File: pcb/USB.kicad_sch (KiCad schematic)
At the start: 101 parts, among them J0 12401598E4#2A, J2 1003-002-01100, J3 1003-002-01100, J4 12401598E4#2A, J5 12401598E4#2A, U0 USBLC6-2SC6, U10 AP22811AW5-7, U11 PTN5110NHQZ, U12 PTN5110NHQZ, U13 PTN5110NHQZ, U14 SN74LVC1G08DCKR, U15 CBTL02043ABQ,115, U19 SN74LVC1G08DCKR, U2 USB7206T/KDX, U20 AP22811AW5-7, U21 USBLC6-2SC6, U23 AP22811AW5-7, U3 CBTL02043ABQ,115, U5 USBLC6-2SC6, U6 CBTL02043ABQ,115, U7 USBLC6-2SC6, U8 USBLC6-2SC6, U9 AP22811AW5-7, X1 ECS-3225MV-250-BN-TR

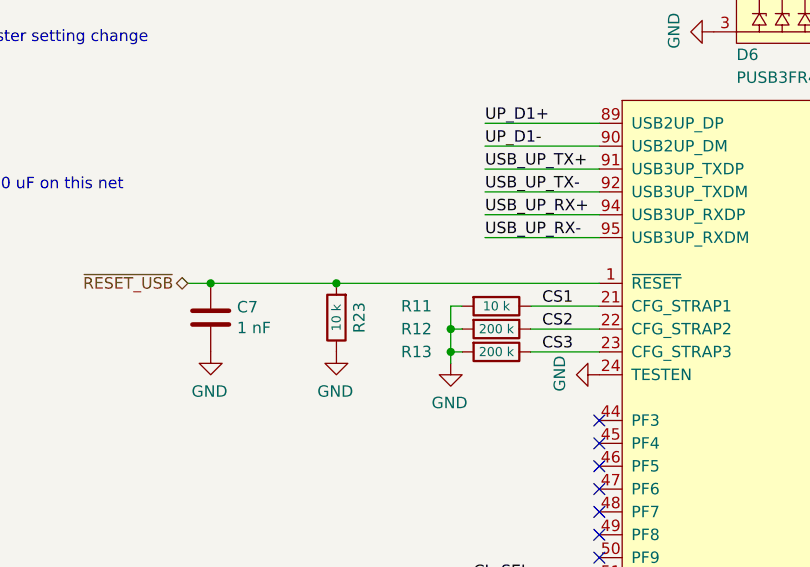
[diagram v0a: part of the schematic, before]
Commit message: hub reset handled by DC-DC power good switch to TLV62585P DC-DC for power good remove reset button - can just plug cable add buttons to ground SDA, SCL as hub bypass to allow programming
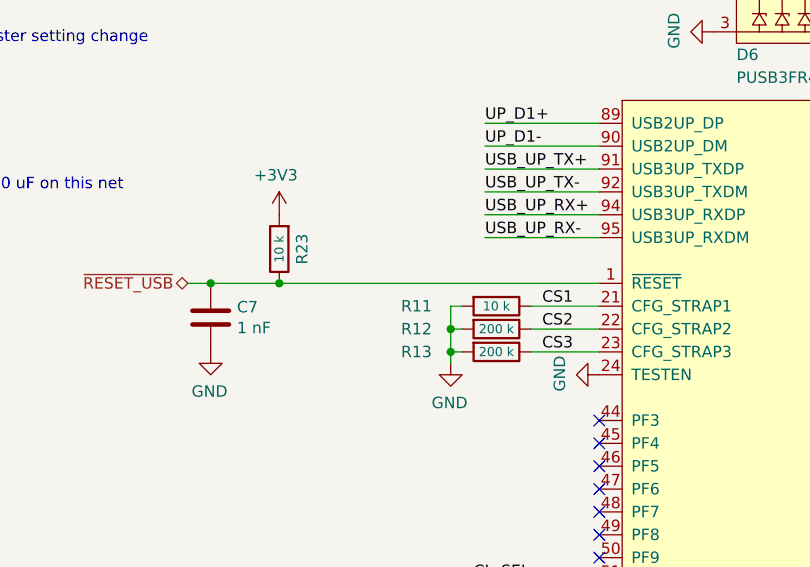
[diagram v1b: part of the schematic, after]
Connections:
- net +3V3: now also R23.2
- net GND: no longer R23.1
- net ~{RESET_USB}: now also R23.1; no longer R23.2
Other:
- moved on the sheet: R23
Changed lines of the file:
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@@
   (junction (at 208.28 226.06) (diameter 0) (color 0 0 0 0)
   )
-  (junction (at 158.75 86.36) (diameter 0) (color 0 0 0 0)
-  )
   (junction (at 377.19 87.63) (diameter 0) (color 0 0 0 0)
   )
@@
   (junction (at 247.65 168.91) (diameter 0) (color 0 0 0 0)
   )
+  (junction (at 152.4 86.36) (diameter 0) (color 0 0 0 0)
+  )
   (junction (at 355.6 46.99) (diameter 0) (color 0 0 0 0)
   )
@@
     (stroke (width 0) (type default))
   )
-  (wire (pts (xy 144.78 86.36) (xy 158.75 86.36))
+  (wire (pts (xy 144.78 86.36) (xy 152.4 86.36))
     (stroke (width 0) (type default))
   )
@@
     (stroke (width 0) (type default))
   )
-  (wire (pts (xy 158.75 86.36) (xy 187.96 86.36))
+  (wire (pts (xy 152.4 86.36) (xy 187.96 86.36))
     (stroke (width 0) (type default))
   )
@@
     )
   )
-  (symbol (lib_id "Device:R") (at 158.75 90.17 180) (unit 1)
+  (symbol (lib_id "Device:R") (at 152.4 82.55 180) (unit 1)
     (in_bom yes) (on_board yes) (dnp no)
-    (property "Reference" "R23" (at 161.29 90.17 90)
+    (property "Reference" "R23" (at 154.94 82.55 90)
       (effects (font (size 1.27 1.27)))
     )
-    (property "Value" "10 k" (at 158.75 90.17 90)
+    (property "Value" "10 k" (at 152.4 82.55 90)
       (effects (font (size 1.016 1.016)))
     )
-    (property "Footprint" "launch:R_0402_1005Metric" (at 160.528 90.17 90)
+    (property "Footprint" "launch:R_0402_1005Metric" (at 154.178 82.55 90)
       (effects (font (size 1.27 1.27)) hide)
     )
-    (property "Datasheet" "~" (at 158.75 90.17 0)
+    (property "Datasheet" "~" (at 152.4 82.55 0)
       (effects (font (size 1.27 1.27)) hide)
     )
-    (property "Manufacturer" "Generic 1% resistor" (at 158.75 90.17 0)
+    (property "Manufacturer" "Generic 1% resistor" (at 152.4 82.55 0)
       (effects (font (size 1.27 1.27)) hide)
     )
@@
     )
   )
-  (symbol (lib_id "power:GND") (at 158.75 93.98 0) (mirror y) (unit 1)
+  (symbol (lib_id "power:+3V3") (at 152.4 78.74 0) (mirror y) (unit 1)
     (in_bom yes) (on_board yes) (dnp no)
-    (property "Reference" "#PWR0279" (at 158.75 100.33 0)
+    (property "Reference" "#PWR02" (at 152.4 82.55 0)
       (effects (font (size 1.27 1.27)) hide)
     )
-    (property "Value" "GND" (at 158.623 98.3742 0)
+    (property "Value" "+3V3" (at 152.019 74.3458 0)
       (effects (font (size 1.27 1.27)))
     )
-    (property "Footprint" "" (at 158.75 93.98 0)
+    (property "Footprint" "" (at 152.4 78.74 0)
       (effects (font (size 1.27 1.27)) hide)
     )
-    (property "Datasheet" "" (at 158.75 93.98 0)
+    (property "Datasheet" "" (at 152.4 78.74 0)
       (effects (font (size 1.27 1.27)) hide)
     )
@@
       (project "launch"
         (path "/80c969df-cd39-4c4a-8336-5a366308cfd3/00000000-0000-0000-0000-00005f58df7c"
-          (reference "#PWR0279") (unit 1)
+          (reference "#PWR02") (unit 1)
         )
       )

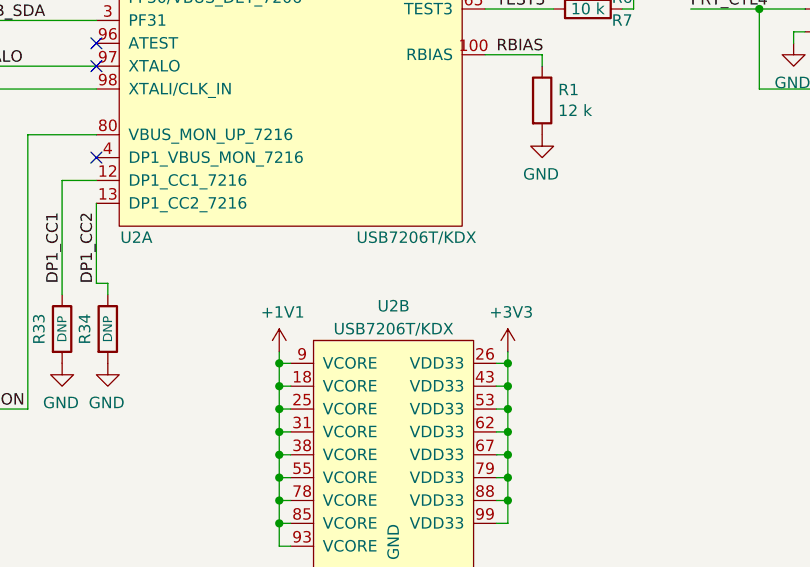
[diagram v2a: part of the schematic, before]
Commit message: BOM update USB7206CT/KDX, TLV62585PDRLR
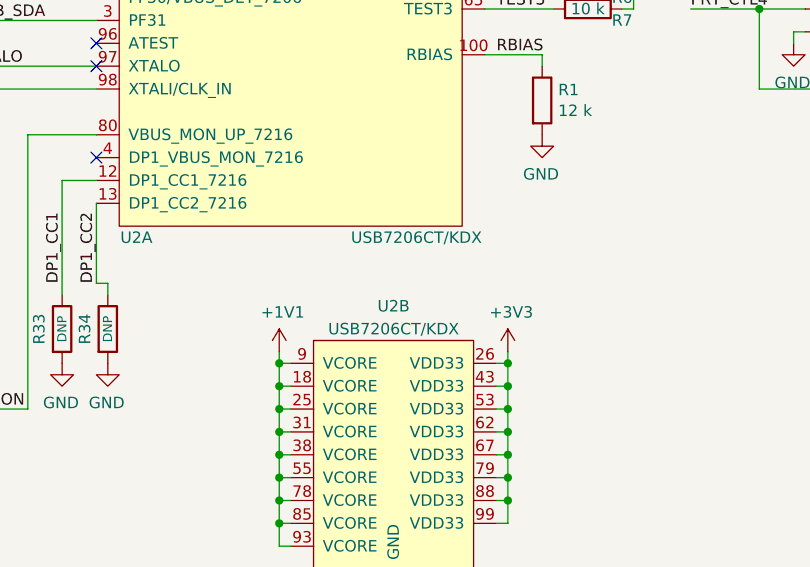
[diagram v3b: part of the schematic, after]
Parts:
- U2: value USB7206T/KDX -> USB7206CT/KDX
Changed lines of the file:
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@@
       (effects (font (size 1.27 1.27)))
     )
-    (property "Value" "USB7206T/KDX" (at 223.52 196.85 0)
+    (property "Value" "USB7206CT/KDX" (at 223.52 196.85 0)
       (effects (font (size 1.27 1.27)))
     )
@@
       (effects (font (size 1.27 1.27)))
     )
-    (property "Value" "USB7206T/KDX" (at 220.98 207.01 0)
+    (property "Value" "USB7206CT/KDX" (at 220.98 207.01 0)
       (effects (font (size 1.27 1.27)))
     )

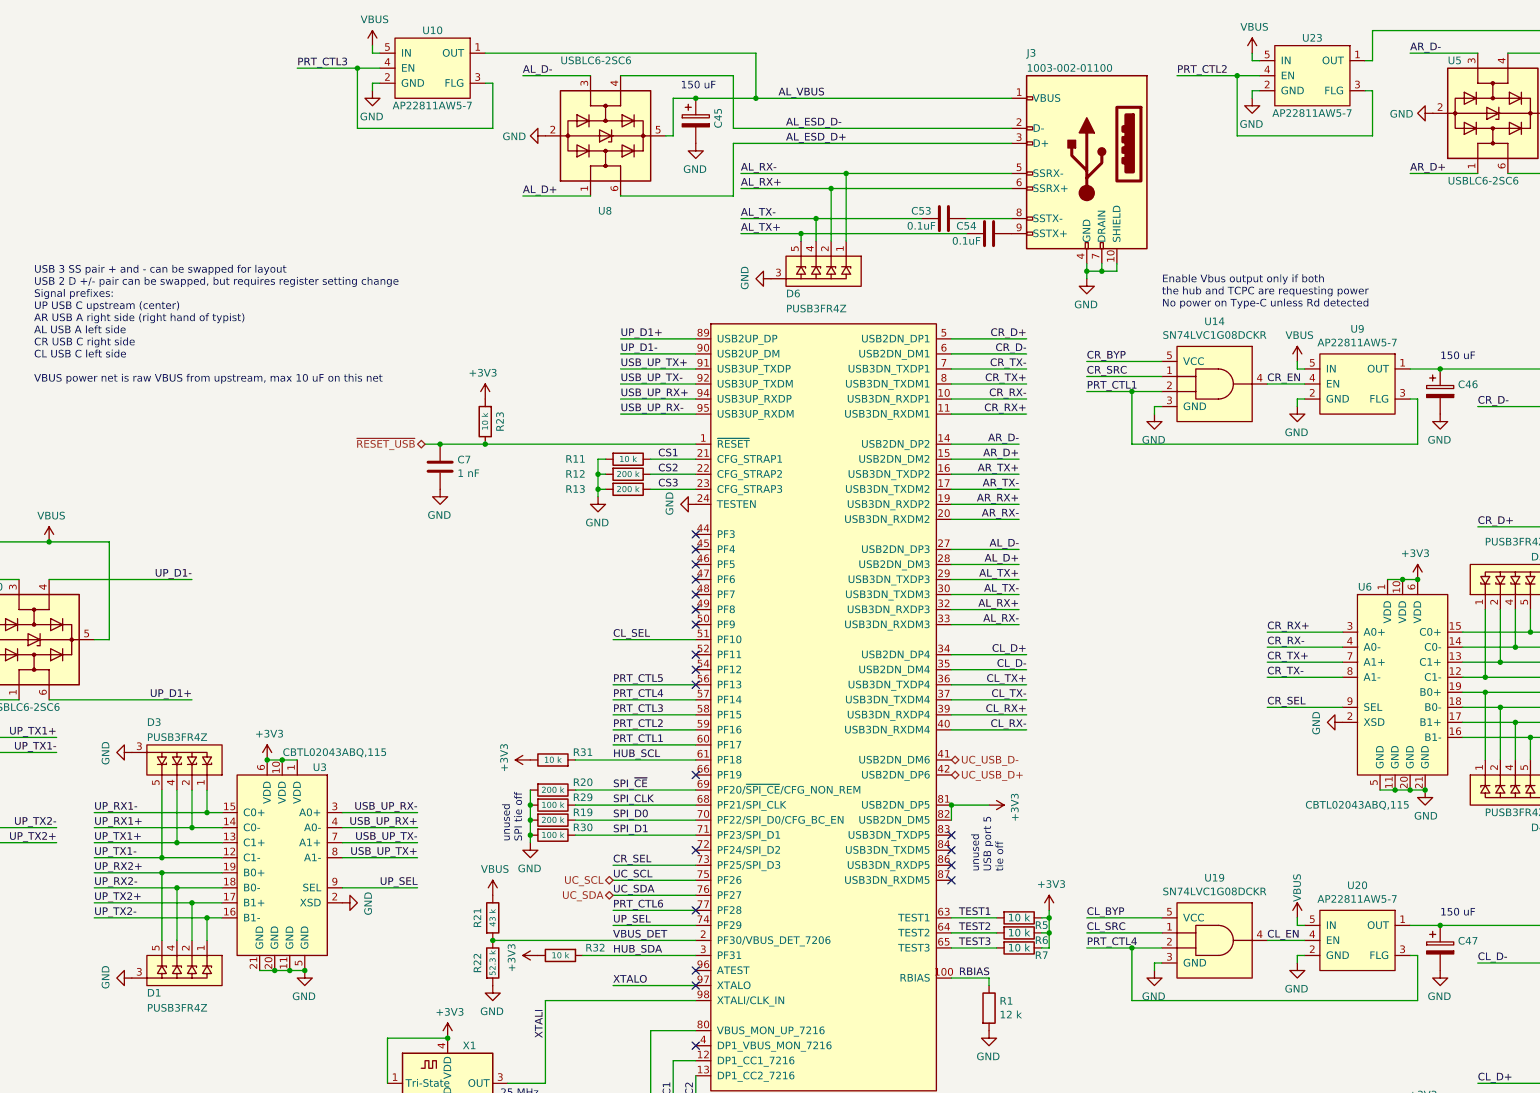
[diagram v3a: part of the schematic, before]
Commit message: VBUS protection circuitry add capacitors at every USB power switch add reverse protection schottky diode     to clamp observed negative voltages seen on VBUS during plug and unplug add RC snubber to VBUS
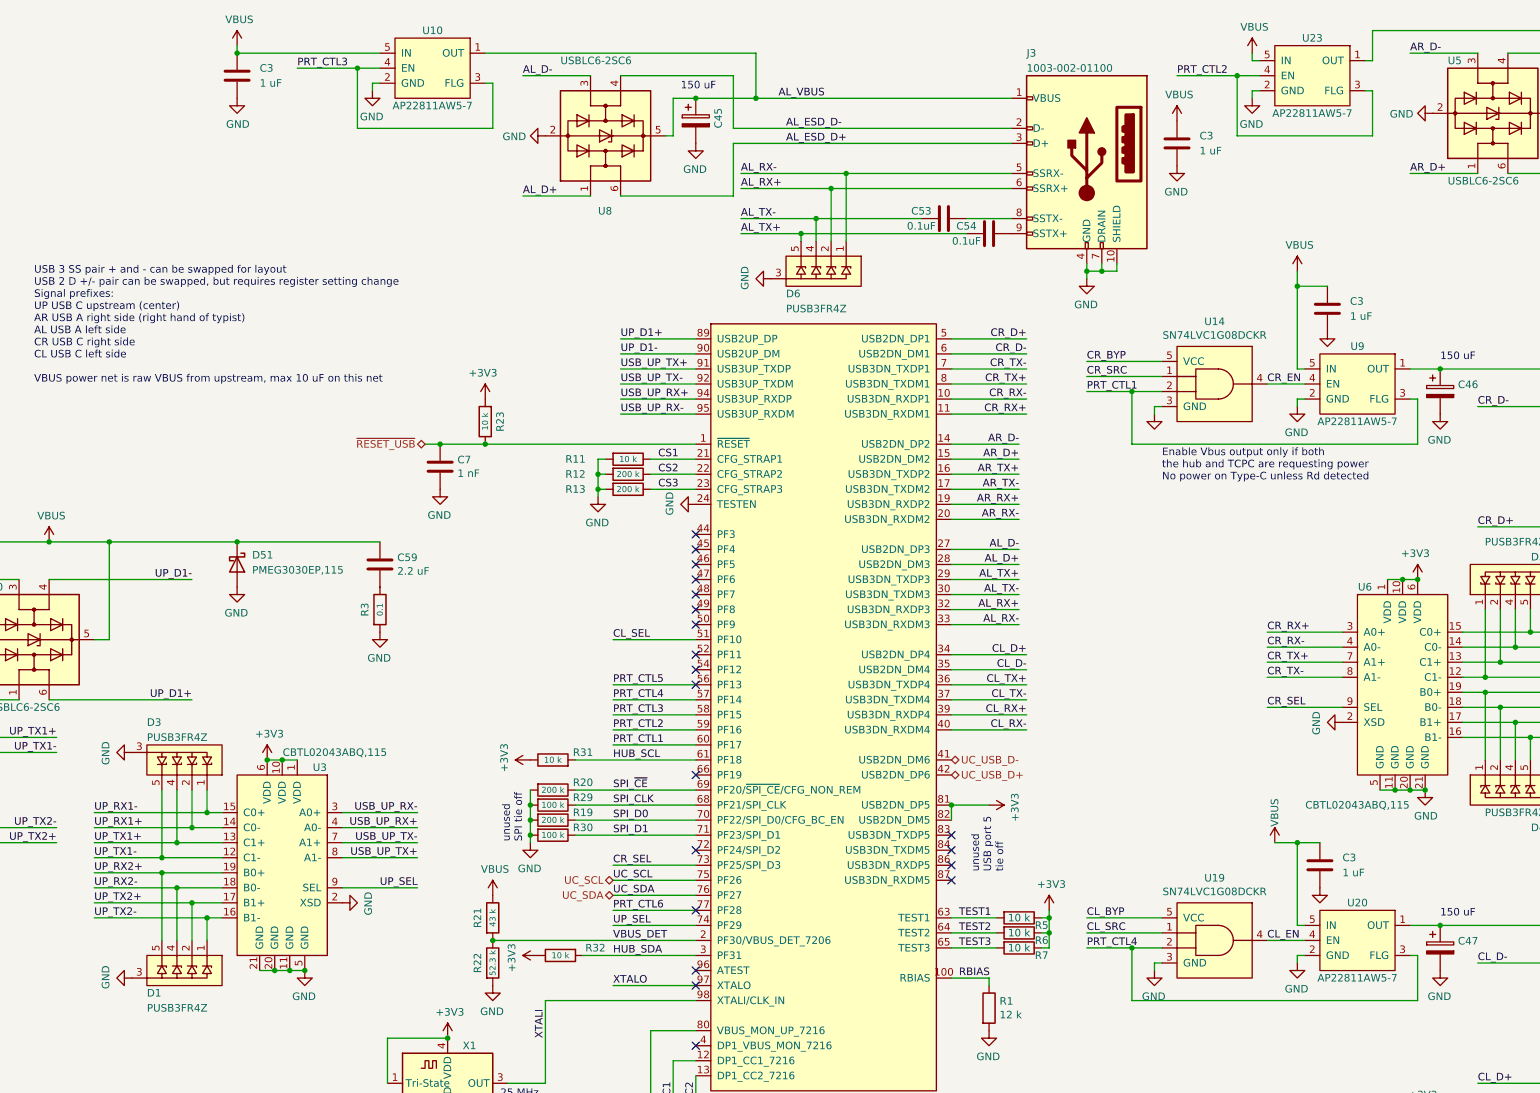
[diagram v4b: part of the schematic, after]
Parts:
- added C3 (x4): 1 uF, launch:C_0402_1005Metric, symbol Device:C
- added C59: 2.2 uF, Capacitor_SMD:C_0603_1608Metric, symbol Device:C
- added D51: PMEG3030EP,115, Diode_SMD:D_SOD-128, symbol Device:D_Schottky
- added R3: 0.1, Resistor_SMD:R_0603_1608Metric, symbol Device:R
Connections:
- net GND: now also C3.2, C3.2, C3.2, C3.2, D51.2 (A), R3.2
- net VBUS: now also C3.1, C3.1, C3.1, C3.1, C59.1, D51.1 (K)
- new net: C59.2, R3.1
